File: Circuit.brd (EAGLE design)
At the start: 99 x 72.1 mm, 114 parts, among them IC1 LM1117T-3.3-V

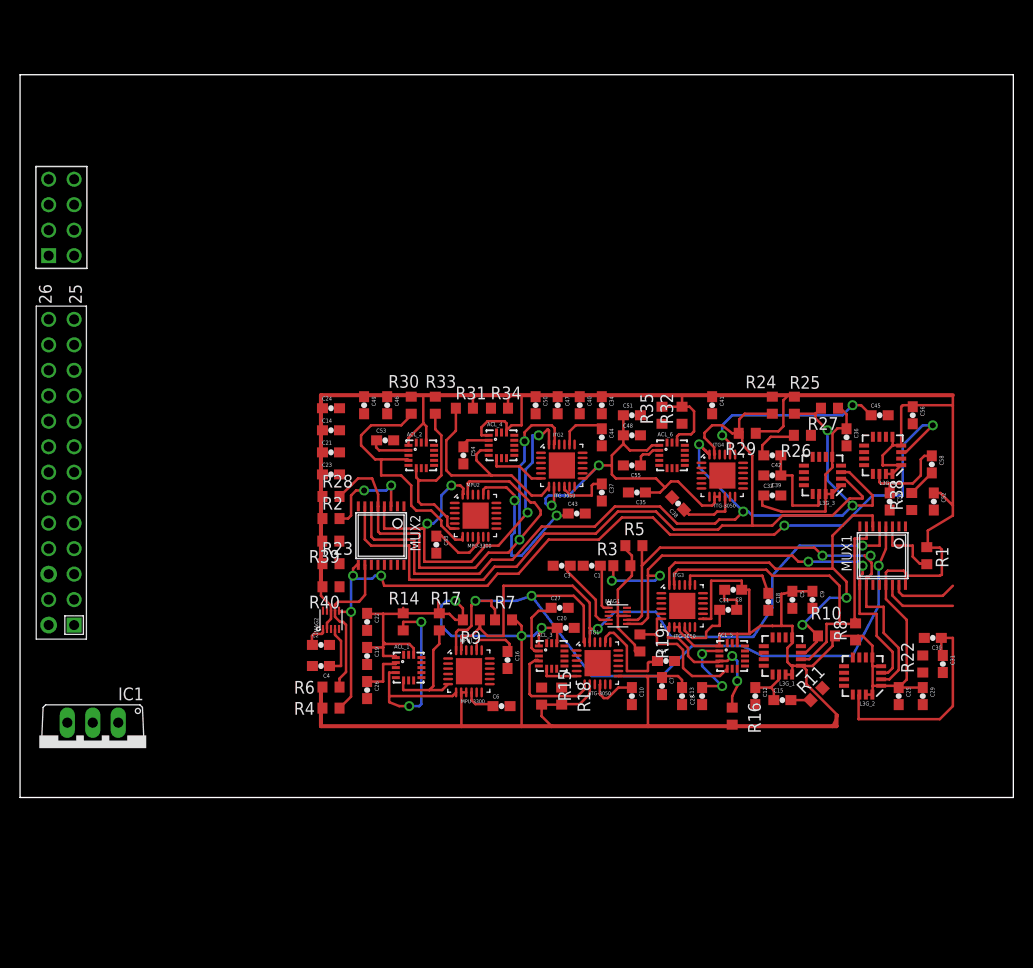
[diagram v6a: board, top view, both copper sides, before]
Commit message: Changed to smashed raspi headers
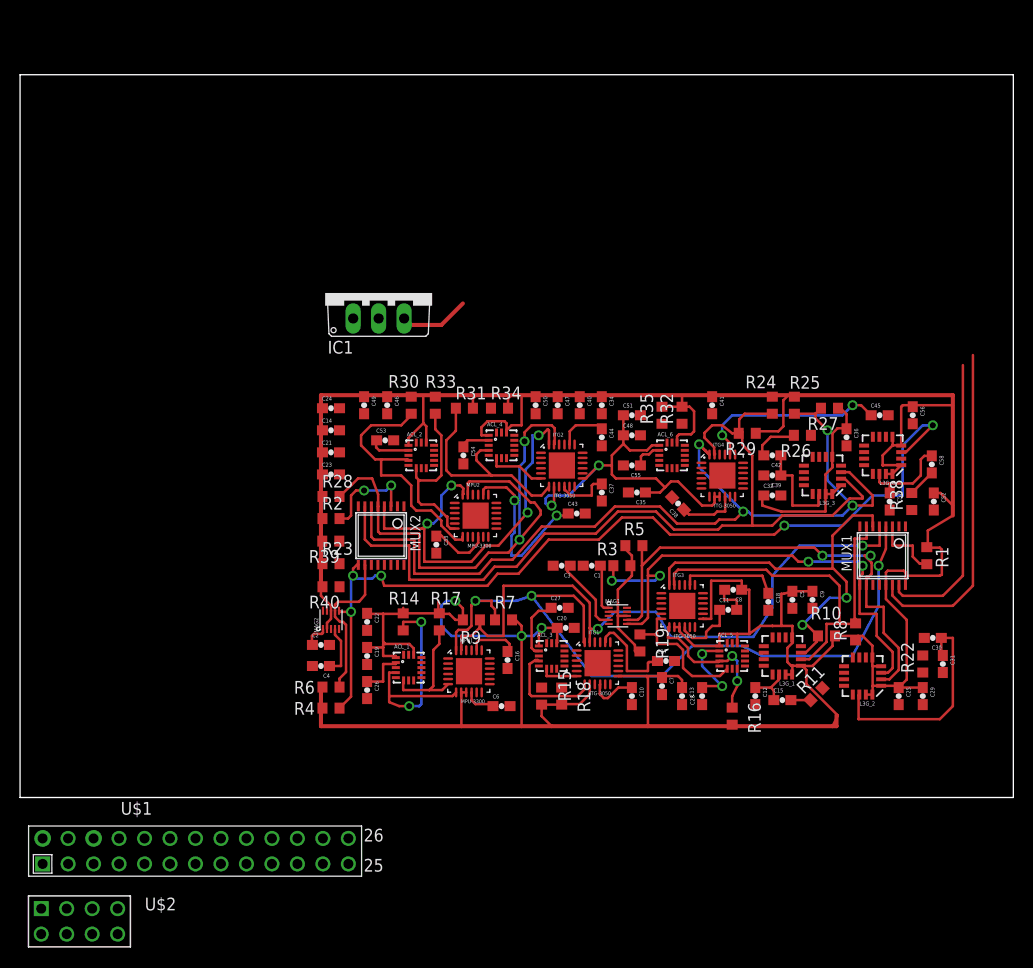
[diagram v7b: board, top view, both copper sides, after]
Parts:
- removed U$3: RASPBERRY-PI_REV2, RaspberryPi:RASPBERRY-PI_REV2
- added U$1: RASPI-P1RASPI_REV2_P1, Gyros:RASPBERRY-PI_REV2
- added U$2: RASPI_P5, RaspberryPi:RASPI_P5
- moved IC1 53.6 mm to (35.8, 50.2), turned to 0 degrees
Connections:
- net CLK1: now also U$1.P1_7; no longer U$3.P1_5
- net CLK2: now also U$2.P5_6; no longer U$3.P5_4
- net GND: now also U$1.P1_16; no longer U$3.P1_14
- net N$10: now also U$1.P1_4; no longer U$3.P1_2
- net SDA1: now also U$1.P1_5; no longer U$3.P1_3
- net SDA2: now also U$2.P5_5; no longer U$3.P5_3
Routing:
- net CLK1: track 7.51 -> 33.3 mm
- net SDA1: track 6.65 -> 29.1 mm
- net +3V3: track 555.6 -> 567.6 mm
- net N$10: track 0.00 -> 7.02 mm
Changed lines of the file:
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@@
 </autorouter>
 <elements>
-<element name="U$3" library="RaspberryPi" package="RASPBERRY-PI_REV2" value="RASPBERRY-PI_REV2" x="6.66" y="48.83" smashed="yes" rot="R90">
-<attribute name="VALUE" x="9.375" y="15.805" size="1.27" layer="27" ratio="10" rot="R90"/>
-</element>
 <element name="MPU1" library="Gyros" package="QFN-24-4MM2" value="MPU-3300" x="44.74" y="12.49"/>
 <element name="ITG1" library="Gyros" package="QFN-24-4MM2" value="ITG-3050" x="57.56" y="13.29"/>
@@
 <attribute name="VALUE" x="44.111" y="15.568" size="1.27" layer="27"/>
 </element>
-<element name="IC1" library="Gyros" package="TO220V" value="LM1117T-3.3-V" x="7.25" y="4.81" rot="R180"/>
+<element name="IC1" library="Gyros" package="TO220V" value="LM1117T-3.3-V" x="35.75" y="50.19"/>
 <element name="R39" library="resistor" package="R0603" value="2.2K" x="30.98" y="25.45" rot="R180"/>
 <element name="R40" library="resistor" package="R0603" value="2.2K" x="31" y="20.9" rot="R180"/>
@@
 <element name="R27" library="resistor" package="R0603" value="2.2K" x="80.7" y="38.7" rot="R180"/>
 <element name="R29" library="resistor" package="R0603" value="2.2K" x="72.5" y="36.2" rot="R180"/>
+<element name="U$1" library="Gyros" package="RASPBERRY-PI_REV2" value="RASPI-P1RASPI_REV2_P1" x="34" y="-8"/>
+<element name="U$2" library="RaspberryPi" package="RASPI_P5" value="RASPI_P5" x="11" y="-15"/>
 </elements>
 <signals>
@@
 <contactref element="ITG3" pad="18"/>
 <contactref element="IC1" pad="1"/>
-<contactref element="U$3" pad="P1_14"/>
 <wire x1="70.25" y1="20.6" x2="70.2" y2="20.6" width="0.254" layer="1"/>
 <wire x1="70.2" y1="20.6" x2="70.2" y2="19.6" width="0.254" layer="1"/>
 <wire x1="70.2" y1="19.6" x2="71.45" y2="19.6" width="0.254" layer="1"/>
 <wire x1="71.45" y1="19.6" x2="71.45" y2="18.6" width="0.254" layer="1"/>
+<contactref element="U$1" pad="P1_16"/>
 <wire x1="86.55" y1="38" x2="89" y2="37.15" width="0" layer="19" extent="1-1"/>
 <wire x1="85.025" y1="35.85" x2="86.55" y2="38" width="0" layer="19" extent="1-1"/>
@@
 <wire x1="90" y1="12.35" x2="90" y2="9.15" width="0" layer="19" extent="1-1"/>
 <wire x1="90.15" y1="15.8" x2="90" y2="12.35" width="0" layer="19" extent="1-1"/>
-<wire x1="9.79" y1="7.35" x2="29.15" y2="13" width="0" layer="19" extent="1-1"/>
-<wire x1="2.85" y1="32.32" x2="9.79" y2="7.35" width="0" layer="19" extent="1-1"/>
+<wire x1="33.21" y1="47.65" x2="31.85" y2="38.7" width="0" layer="19" extent="1-1"/>
+<wire x1="20.03" y1="-4.19" x2="29.15" y2="13" width="0" layer="19" extent="1-1"/>
 </signal>
 <signal name="CLK1">
-<contactref element="U$3" pad="P1_5"/>
 <contactref element="MUX1" pad="14"/>
 <wire x1="86.975" y1="21.0822" x2="86.975" y2="20.025" width="0.254" layer="1"/>
 <wire x1="86.975" y1="20.025" x2="88" y2="19" width="0.254" layer="1"/>
 <wire x1="88" y1="19" x2="93" y2="19" width="0.254" layer="1"/>
-<wire x1="5.39" y1="22.16" x2="86.975" y2="21.0822" width="0" layer="19" extent="1-1"/>
+<wire x1="95" y1="44" x2="95" y2="21" width="0.254" layer="1"/>
+<wire x1="95" y1="21" x2="93" y2="19" width="0.254" layer="1"/>
+<contactref element="U$1" pad="P1_7"/>
+<wire x1="9.87" y1="-6.73" x2="86.975" y2="20.025" width="0" layer="19" extent="1-1"/>
 </signal>
 <signal name="SDA1">
-<contactref element="U$3" pad="P1_3"/>
 <contactref element="MUX1" pad="15"/>
 <wire x1="87.625" y1="21.0822" x2="87.625" y2="20.375" width="0.254" layer="1"/>
 <wire x1="87.625" y1="20.375" x2="88" y2="20" width="0.254" layer="1"/>
 <wire x1="88" y1="20" x2="92" y2="20" width="0.254" layer="1"/>
-<wire x1="92" y1="20" x2="93" y2="21" width="0.254" layer="1"/>
-<wire x1="5.39" y1="19.62" x2="87.625" y2="21.0822" width="0" layer="19" extent="1-1"/>
+<wire x1="94" y1="43" x2="94" y2="22" width="0.254" layer="1"/>
+<wire x1="94" y1="22" x2="92" y2="20" width="0.254" layer="1"/>
+<contactref element="U$1" pad="P1_5"/>
+<wire x1="7.33" y1="-6.73" x2="87.625" y2="20.375" width="0" layer="19" extent="1-1"/>
 </signal>
 <signal name="SDA2">
-<contactref element="U$3" pad="P5_3"/>
 <contactref element="MUX2" pad="15"/>
 <contactref element="R39" pad="1"/>
-<wire x1="31.83" y1="25.45" x2="2.85" y2="56.45" width="0" layer="19" extent="1-1"/>
-<wire x1="37.625" y1="23.0822" x2="31.83" y2="25.45" width="0" layer="19" extent="1-1"/>
+<contactref element="U$2" pad="P5_5"/>
+<wire x1="31.83" y1="25.45" x2="37.625" y2="23.0822" width="0" layer="19" extent="1-1"/>
+<wire x1="7.19" y1="-11.19" x2="31.83" y2="25.45" width="0" layer="19" extent="1-1"/>
 </signal>
 <signal name="N$3">
@@
 <wire x1="30.6" y1="17.3" x2="31" y2="17.7" width="0.254" layer="1"/>
 <wire x1="31" y1="17.7" x2="31" y2="18.51" width="0.254" layer="1"/>
+<wire x1="93" y1="40" x2="93" y2="28" width="0.4064" layer="1"/>
 <wire x1="89" y1="39" x2="89" y2="38.85" width="0" layer="19" extent="1-1"/>
 <wire x1="63.725" y1="35" x2="65.5" y2="35.275" width="0" layer="19" extent="1-1"/>
@@
 <wire x1="45.1425" y1="25.8784" x2="47.4862" y2="26.7033" width="0" layer="19" extent="1-1"/>
 <wire x1="44.6379" y1="25.8784" x2="45.1425" y2="25.8784" width="0" layer="19" extent="1-1"/>
-<wire x1="7.25" y1="7.35" x2="30" y2="7" width="0" layer="19" extent="1-1"/>
+<wire x1="35.75" y1="47.65" x2="34" y2="40" width="0" layer="19" extent="1-1"/>
 </signal>
 <signal name="M1_AUXSDA">
@@
 <signal name="CLK2">
 <contactref element="MUX2" pad="14"/>
-<contactref element="U$3" pad="P5_4"/>
 <contactref element="R40" pad="1"/>
-<wire x1="31.85" y1="20.9" x2="5.39" y2="56.45" width="0" layer="19" extent="1-1"/>
-<wire x1="36.975" y1="23.0822" x2="31.85" y2="20.9" width="0" layer="19" extent="1-1"/>
+<contactref element="U$2" pad="P5_6"/>
+<wire x1="31.85" y1="20.9" x2="36.975" y2="23.0822" width="0" layer="19" extent="1-1"/>
+<wire x1="7.19" y1="-13.73" x2="31.85" y2="20.9" width="0" layer="19" extent="1-1"/>
 </signal>
 <signal name="N$9">
@@
 <wire x1="34.4" y1="20.1" x2="34.4" y2="23.0572" width="0.254" layer="1"/>
 <wire x1="34.4" y1="23.0572" x2="34.375" y2="23.0822" width="0.254" layer="1"/>
-<wire x1="34.4" y1="23.0572" x2="87.85" y2="33.675" width="0" layer="19" extent="1-1"/>
 <wire x1="31.85" y1="10.9" x2="31.85" y2="11.75" width="0.254" layer="1"/>
 <wire x1="31.85" y1="11.75" x2="32.5" y2="12.4" width="0.254" layer="1"/>
@@
 <wire x1="31.9" y1="17.4" x2="31.4" y2="17.9" width="0.254" layer="1"/>
 <wire x1="31.4" y1="17.9" x2="31.4" y2="18.51" width="0.254" layer="1"/>
+<wire x1="34.4" y1="23.0572" x2="87.85" y2="33.675" width="0" layer="19" extent="1-1"/>
 </signal>
 <signal name="B2_SD2">
@@
 </signal>
 <signal name="N$10">
-<contactref element="U$3" pad="P1_2"/>
 <contactref element="IC1" pad="3"/>
-<wire x1="4.71" y1="7.35" x2="2.85" y2="17.08" width="0" layer="19" extent="1-1"/>
+<wire x1="44.15" y1="49.15" x2="42" y2="47" width="0.4064" layer="1"/>
+<wire x1="42" y1="47" x2="38.94" y2="47" width="0.4064" layer="1"/>
+<wire x1="38.94" y1="47" x2="38.29" y2="47.65" width="0.4064" layer="1"/>
+<contactref element="U$1" pad="P1_4"/>
+<wire x1="4.79" y1="-4.19" x2="38.94" y2="47" width="0" layer="19" extent="1-1"/>
 </signal>
 </signals>

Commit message: Prior to removal of interupt wires
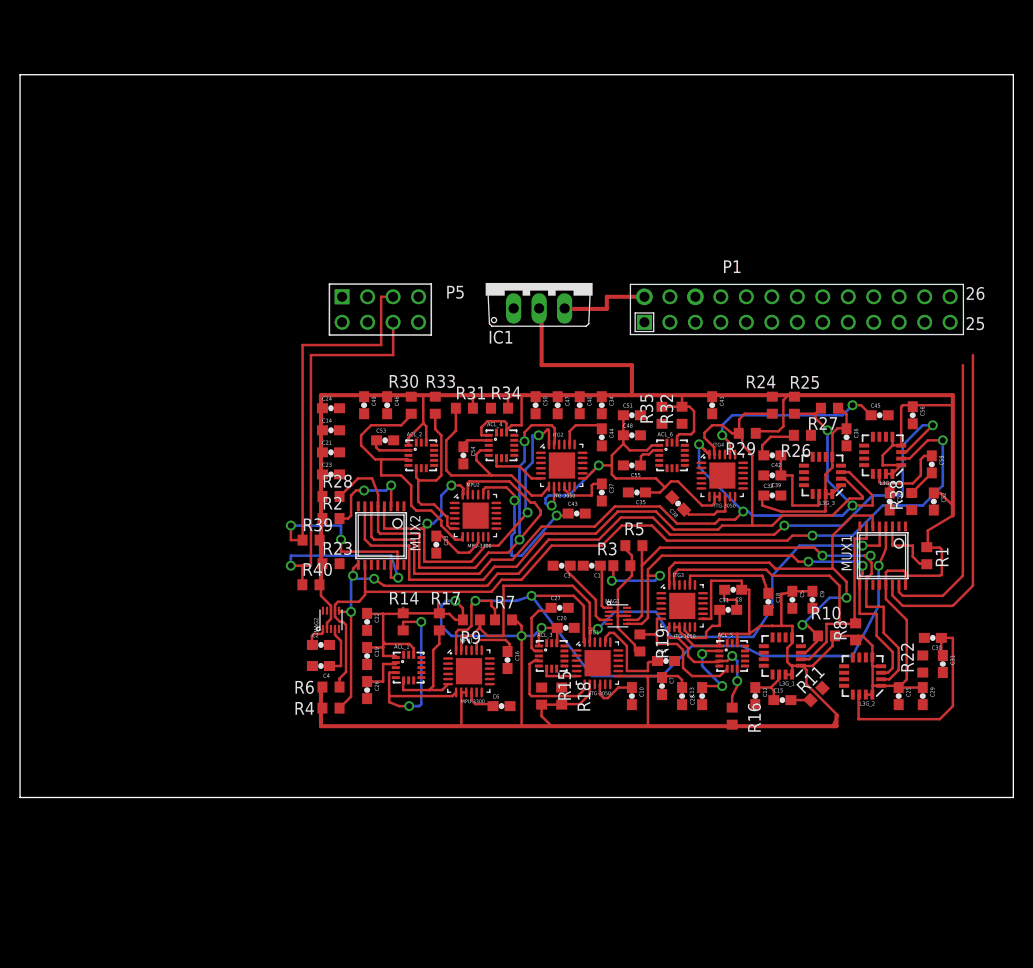
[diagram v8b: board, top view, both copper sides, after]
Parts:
- removed U$1: RASPI-P1RASPI_REV2_P1, Gyros:RASPBERRY-PI_REV2
- removed U$2: RASPI_P5, RaspberryPi:RASPI_P5
- added P1: RASPI-P1RASPI_REV2_P1, Gyros:RASPBERRY-PI_REV2
- added P5: RASPI_P5, RaspberryPi:RASPI_P5
- moved IC1 16.0 mm to (51.8, 51.2)
- moved R40 2.01 mm to (29.0, 21.1), turned to 0 degrees
- moved R39 1.96 mm to (29.0, 25.6), turned to 0 degrees
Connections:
- net CLK1: now also P1.P1_7; no longer U$1.P1_7
- net CLK2: now also P5.P5_6; no longer U$2.P5_6
- net GND: now also P1.P1_14; no longer U$1.P1_16
- net N$10: now also P1.P1_2; no longer U$1.P1_4
- net SDA1: now also P1.P1_5; no longer U$1.P1_5
- net SDA2: now also P5.P5_5; no longer U$2.P5_5
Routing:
- net B2_SC2: track 15.5 -> 88.4 mm, vias 0 -> 2
- net CLK2: track 0.00 -> 51.7 mm, vias 0 -> 2
- net SDA2: track 0.00 -> 50.4 mm, vias 0 -> 2
- net +3V3: track 567.6 -> 586.0 mm
- net N$10: track 7.02 -> 9.22 mm
- net B2_SD2: track 90.6 -> 89.9 mm
